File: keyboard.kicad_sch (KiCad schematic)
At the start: 10 parts

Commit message: Fix wrong cap type in clock generator
Also fill some references automatically generated by KiCAD.
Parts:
- C18, C24, C25: renamed from C?; value (none) -> 100nF; footprint (none) -> artemisa:Disc_capacitor
- J2: value (none) -> DB25M; footprint (none) -> artemisa:DB25M
- RN2: value (none) -> 10K; footprint (none) -> artemisa:RN8
- U16: renamed from U?; value (none) -> 74LS07; footprint (none) -> artemisa:DIP-14_300
- U21, U22: value (none) -> 74HC138; footprint (none) -> artemisa:DIP-16_300
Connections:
- net ~{KANALOCK}: now also U16.13; no longer U16.11
- net ~{KANAL}: now also U16.12; no longer U16.10
- net VCC: now reaches RN2.1
- net VCC: now also C18.1, C24.1, C25.1, J2.23 (Pin_23), U16.14 (VCC), U21.16 (VCC), U21.6 (E3), U22.16 (VCC)
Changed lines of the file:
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@@
       (effects (font (size 1.524 1.524)) (justify left))
     )
-    (property "Value" "" (id 1) (at 103.632 26.7462 0)
+    (property "Value" "10K" (id 1) (at 103.632 26.7462 0)
       (effects (font (size 1.524 1.524)) (justify left))
     )
-    (property "Footprint" "" (id 2) (at 121.92 28.575 0)
+    (property "Footprint" "artemisa:RN8" (id 2) (at 121.92 28.575 0)
       (effects (font (size 1.524 1.524)) hide)
     )
@@
       (effects (font (size 1.27 1.27)) (justify right))
     )
-    (property "Value" "" (id 1) (at 201.3712 81.7118 0)
+    (property "Value" "DB25M" (id 1) (at 201.3712 81.7118 0)
       (effects (font (size 1.27 1.27)) (justify right))
     )
-    (property "Footprint" "" (id 2) (at 200.66 80.01 0)
+    (property "Footprint" "artemisa:DB25M" (id 2) (at 200.66 80.01 0)
       (effects (font (size 1.27 1.27)) hide)
     )
@@
       (effects (font (size 1.524 1.524)) hide)
     )
-    (property "Value" "" (id 1) (at 193.04 39.37 0)
+    (property "Value" "VCC" (id 1) (at 193.04 39.37 0)
       (effects (font (size 1.524 1.524)) hide)
     )
@@
       (effects (font (size 1.524 1.524)) hide)
     )
-    (property "Value" "" (id 1) (at 193.04 110.49 0)
+    (property "Value" "GND" (id 1) (at 193.04 110.49 0)
       (effects (font (size 1.524 1.524)) hide)
     )
@@
       (effects (font (size 1.524 1.524)) hide)
     )
-    (property "Value" "" (id 1) (at 114.3 11.43 0)
+    (property "Value" "VCC" (id 1) (at 114.3 11.43 0)
       (effects (font (size 1.524 1.524)) hide)
     )
@@
   (symbol (lib_id "artemisa:74LS07") (at 115.57 134.62 0) (unit 5)
     (in_bom yes) (on_board yes)
-    (property "Reference" "U?" (id 0) (at 110.49 130.81 0))
-    (property "Value" "" (id 1) (at 118.11 130.81 0))
-    (property "Footprint" "" (id 2) (at 115.57 134.62 0)
+    (property "Reference" "U16" (id 0) (at 110.49 130.81 0))
+    (property "Value" "74LS07" (id 1) (at 118.11 130.81 0))
+    (property "Footprint" "artemisa:DIP-14_300" (id 2) (at 115.57 134.62 0)
       (effects (font (size 1.27 1.27)) hide)
     )
@@
     (pin "7")
   )
-  (symbol (lib_id "artemisa:74LS07") (at 115.57 142.24 0) (unit 5)
-    (in_bom yes) (on_board yes)
-    (property "Reference" "U?" (id 0) (at 110.49 138.43 0))
-    (property "Value" "" (id 1) (at 118.11 138.43 0))
-    (property "Footprint" "" (id 2) (at 115.57 142.24 0)
+  (symbol (lib_id "artemisa:74LS07") (at 115.57 142.24 0) (unit 6)
+    (in_bom yes) (on_board yes)
+    (property "Reference" "U16" (id 0) (at 110.49 138.43 0))
+    (property "Value" "74LS07" (id 1) (at 118.11 138.43 0))
+    (property "Footprint" "artemisa:DIP-14_300" (id 2) (at 115.57 142.24 0)
       (effects (font (size 1.27 1.27)) hide)
     )
@@
       (effects (font (size 1.524 1.524)))
     )
-    (property "Value" "" (id 1) (at 143.51 80.01 0)
+    (property "Value" "74HC138" (id 1) (at 143.51 80.01 0)
       (effects (font (size 1.524 1.524)))
     )
-    (property "Footprint" "" (id 2) (at 115.57 69.85 90)
+    (property "Footprint" "artemisa:DIP-16_300" (id 2) (at 115.57 69.85 90)
       (effects (font (size 1.524 1.524)) hide)
     )
@@
       (effects (font (size 1.524 1.524)))
     )
-    (property "Value" "" (id 1) (at 143.51 120.65 0)
+    (property "Value" "74HC138" (id 1) (at 143.51 120.65 0)
       (effects (font (size 1.524 1.524)))
     )
-    (property "Footprint" "" (id 2) (at 115.57 110.49 90)
+    (property "Footprint" "artemisa:DIP-16_300" (id 2) (at 115.57 110.49 90)
       (effects (font (size 1.524 1.524)) hide)
     )
@@
       (effects (font (size 1.524 1.524)) hide)
     )
-    (property "Value" "" (id 1) (at 137.16 78.74 0)
+    (property "Value" "GND" (id 1) (at 137.16 78.74 0)
       (effects (font (size 1.524 1.524)) hide)
     )
@@
       (effects (font (size 1.524 1.524)) hide)
     )
-    (property "Value" "" (id 1) (at 137.16 82.55 0)
+    (property "Value" "VCC" (id 1) (at 137.16 82.55 0)
       (effects (font (size 1.524 1.524)) hide)
     )
@@
   (symbol (lib_id "artemisa:Cap") (at 144.78 91.44 90) (unit 1)
     (in_bom yes) (on_board yes)
-    (property "Reference" "C?" (id 0) (at 143.51 90.17 90)
-      (effects (font (size 1.27 1.27)) (justify left))
-    )
-    (property "Value" "" (id 1) (at 152.4 90.17 90)
-      (effects (font (size 1.27 1.27)) (justify left))
-    )
-    (property "Footprint" "" (id 2) (at 144.78 91.44 0)
+    (property "Reference" "C25" (id 0) (at 143.51 90.17 90)
+      (effects (font (size 1.27 1.27)) (justify left))
+    )
+    (property "Value" "100nF" (id 1) (at 152.4 90.17 90)
+      (effects (font (size 1.27 1.27)) (justify left))
+    )
+    (property "Footprint" "artemisa:Disc_capacitor" (id 2) (at 144.78 91.44 0)
       (effects (font (size 1.27 1.27)) hide)
     )
@@
       (effects (font (size 1.524 1.524)) hide)
     )
-    (property "Value" "" (id 1) (at 149.86 91.44 0)
+    (property "Value" "GND" (id 1) (at 149.86 91.44 0)
       (effects (font (size 1.524 1.524)) hide)
     )
@@
       (effects (font (size 1.524 1.524)) hide)
     )
-    (property "Value" "" (id 1) (at 110.49 76.2 0)
+    (property "Value" "GND" (id 1) (at 110.49 76.2 0)
       (effects (font (size 1.524 1.524)) hide)
     )
@@
       (effects (font (size 1.524 1.524)) hide)
     )
-    (property "Value" "" (id 1) (at 113.03 62.23 0)
+    (property "Value" "VCC" (id 1) (at 113.03 62.23 0)
       (effects (font (size 1.524 1.524)) hide)
     )
@@
       (effects (font (size 1.524 1.524)) hide)
     )
-    (property "Value" "" (id 1) (at 110.49 116.84 0)
+    (property "Value" "GND" (id 1) (at 110.49 116.84 0)
       (effects (font (size 1.524 1.524)) hide)
     )
@@
       (effects (font (size 1.524 1.524)) hide)
     )
-    (property "Value" "" (id 1) (at 137.16 41.91 0)
+    (property "Value" "VCC" (id 1) (at 137.16 41.91 0)
       (effects (font (size 1.524 1.524)) hide)
     )
@@
   (symbol (lib_id "artemisa:Cap") (at 144.78 50.8 90) (unit 1)
     (in_bom yes) (on_board yes)
-    (property "Reference" "C?" (id 0) (at 143.51 49.53 90)
-      (effects (font (size 1.27 1.27)) (justify left))
-    )
-    (property "Value" "" (id 1) (at 152.4 49.53 90)
-      (effects (font (size 1.27 1.27)) (justify left))
-    )
-    (property "Footprint" "" (id 2) (at 144.78 50.8 0)
+    (property "Reference" "C24" (id 0) (at 143.51 49.53 90)
+      (effects (font (size 1.27 1.27)) (justify left))
+    )
+    (property "Value" "100nF" (id 1) (at 152.4 49.53 90)
+      (effects (font (size 1.27 1.27)) (justify left))
+    )
+    (property "Footprint" "artemisa:Disc_capacitor" (id 2) (at 144.78 50.8 0)
       (effects (font (size 1.27 1.27)) hide)
     )
@@
       (effects (font (size 1.524 1.524)) hide)
     )
-    (property "Value" "" (id 1) (at 149.86 50.8 0)
+    (property "Value" "GND" (id 1) (at 149.86 50.8 0)
       (effects (font (size 1.524 1.524)) hide)
     )
@@
       (effects (font (size 1.524 1.524)) hide)
     )
-    (property "Value" "" (id 1) (at 137.16 119.38 0)
+    (property "Value" "GND" (id 1) (at 137.16 119.38 0)
       (effects (font (size 1.524 1.524)) hide)
     )
@@
   (symbol (lib_id "artemisa:74LS07") (at 241.3 55.88 0) (unit 7)
     (in_bom yes) (on_board yes)
-    (property "Reference" "U?" (id 0) (at 236.22 50.8 90)
-      (effects (font (size 1.27 1.27)) (justify left))
-    )
-    (property "Value" "" (id 1) (at 236.22 64.77 90)
-      (effects (font (size 1.27 1.27)) (justify left))
-    )
-    (property "Footprint" "" (id 2) (at 241.3 55.88 0)
+    (property "Reference" "U16" (id 0) (at 236.22 50.8 90)
+      (effects (font (size 1.27 1.27)) (justify left))
+    )
+    (property "Value" "74LS07" (id 1) (at 236.22 64.77 90)
+      (effects (font (size 1.27 1.27)) (justify left))
+    )
+    (property "Footprint" "artemisa:DIP-14_300" (id 2) (at 241.3 55.88 0)
       (effects (font (size 1.27 1.27)) hide)
     )
@@
   (symbol (lib_id "artemisa:GND") (at 241.3 66.04 0) (unit 1)
     (in_bom yes) (on_board yes)
-    (property "Reference" "#PWR?" (id 0) (at 241.3 68.58 0)
-      (effects (font (size 1.524 1.524)) hide)
-    )
-    (property "Value" "" (id 1) (at 241.3 63.5 0)
+    (property "Reference" "#PWR0158" (id 0) (at 241.3 68.58 0)
+      (effects (font (size 1.524 1.524)) hide)
+    )
+    (property "Value" "GND" (id 1) (at 241.3 63.5 0)
       (effects (font (size 1.524 1.524)) hide)
     )
@@
   (symbol (lib_id "artemisa:VCC") (at 241.3 45.72 0) (unit 1)
     (in_bom yes) (on_board yes)
-    (property "Reference" "#PWR?" (id 0) (at 241.3 46.99 0)
-      (effects (font (size 1.524 1.524)) hide)
-    )
-    (property "Value" "" (id 1) (at 241.3 39.37 0)
+    (property "Reference" "#PWR0159" (id 0) (at 241.3 46.99 0)
+      (effects (font (size 1.524 1.524)) hide)
+    )
+    (property "Value" "VCC" (id 1) (at 241.3 39.37 0)
       (effects (font (size 1.524 1.524)) hide)
     )
@@
   (symbol (lib_id "artemisa:Cap") (at 248.92 55.88 0) (unit 1)
     (in_bom yes) (on_board yes)
-    (property "Reference" "C?" (id 0) (at 250.19 54.61 90)
-      (effects (font (size 1.27 1.27)) (justify left))
-    )
-    (property "Value" "" (id 1) (at 250.19 63.5 90)
-      (effects (font (size 1.27 1.27)) (justify left))
-    )
-    (property "Footprint" "" (id 2) (at 248.92 55.88 0)
-      (effects (font (size 1.27 1.27)) hide)
-    )
+    (property "Reference" "C18" (id 0) (at 250.19 54.61 90)
+      (effects (font (size 1.27 1.27)) (justify left))
+    )
+    (property "Value" "100nF" (id 1) (at 250.19 63.5 90)
+      (effects (font (size 1.27 1.27)) (justify left))
+    )
+    (property "Footprint" "artemisa:Disc_capacitor" (id 2) (at 248.92 55.88 0)
+      (effects (font (size 1.27 1.27)) hide)
+    )

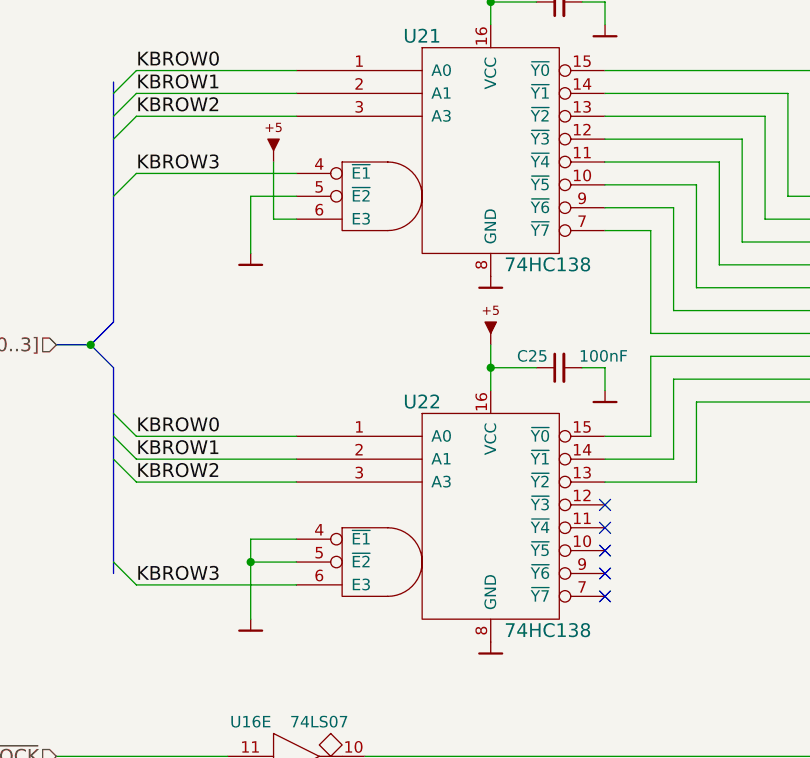
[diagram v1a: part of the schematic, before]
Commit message: Upgrade project files to KiCad v8
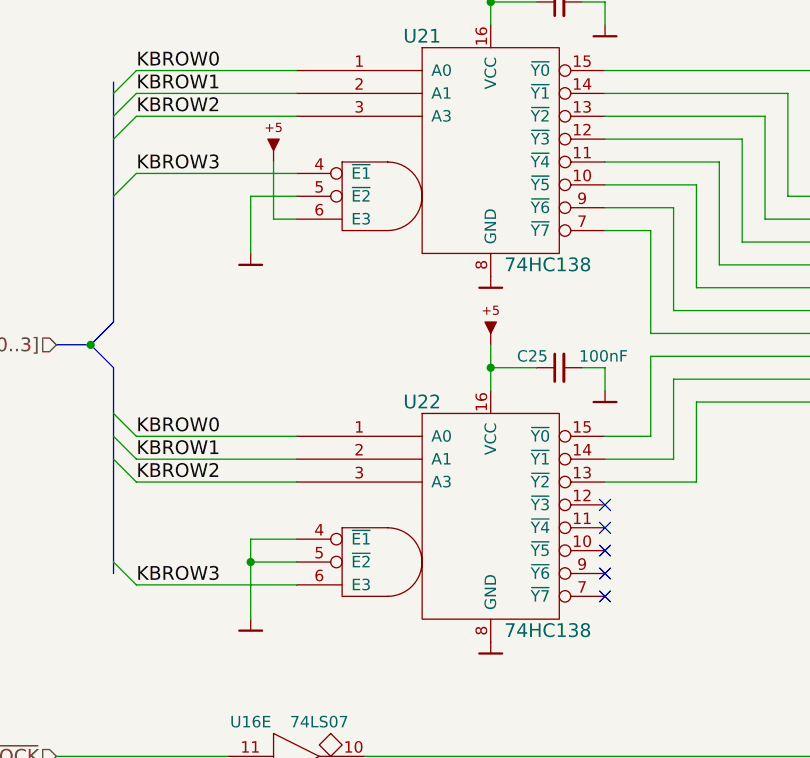
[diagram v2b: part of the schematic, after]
